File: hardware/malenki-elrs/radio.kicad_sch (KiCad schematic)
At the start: 13 parts, among them U3 SX1280IMLTRT, Y2 CRYSTAL 52MHz 10pF SMD

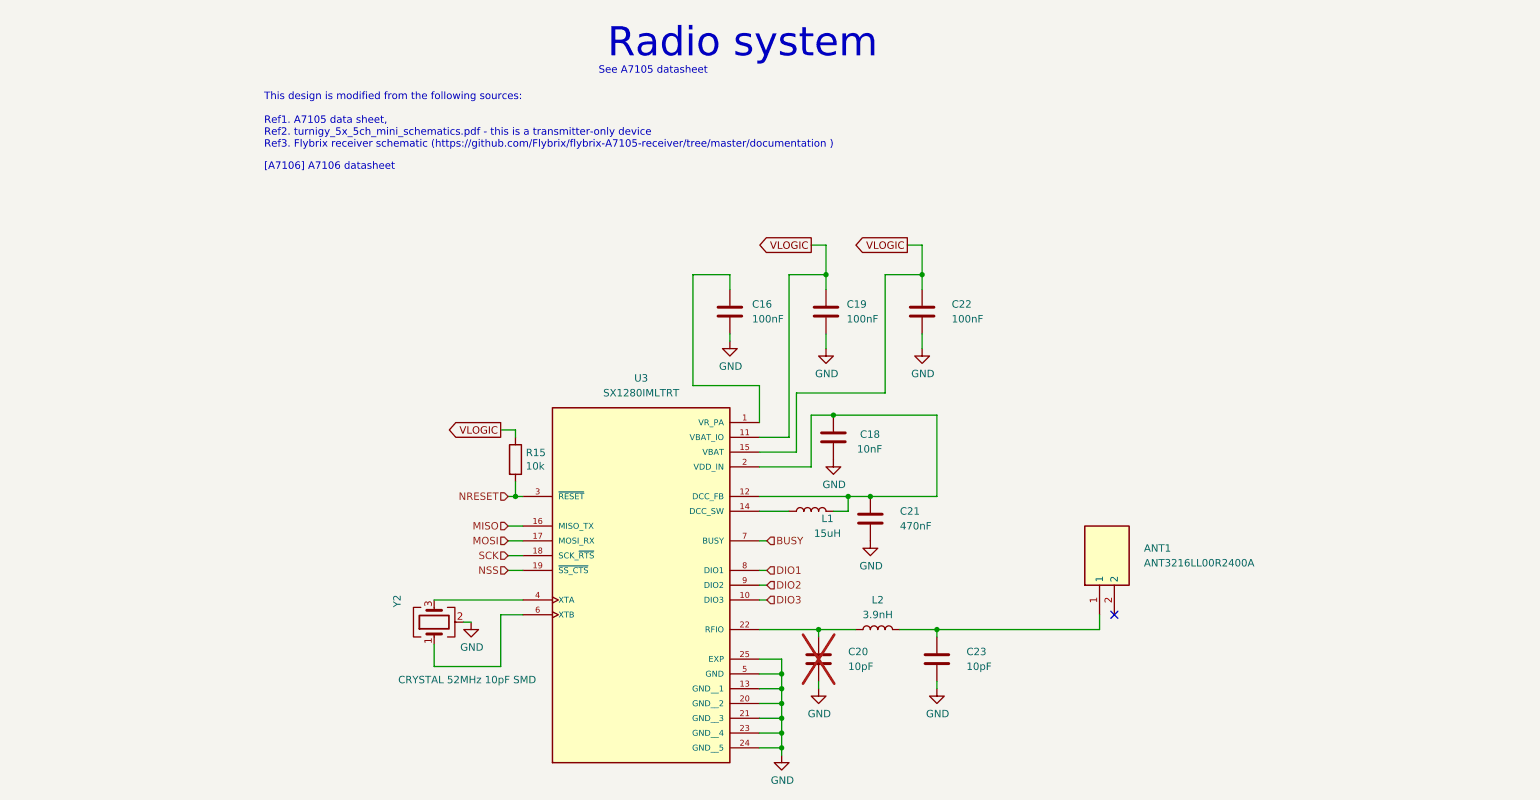
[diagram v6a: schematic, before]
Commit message: Changed microcontroller and completed schematic
Changed micro controller to the esp32-s3FN8, for more available pins.
Complete schematic.
Changed to pcb antenna.
Completed initial placement of all components on PCB.
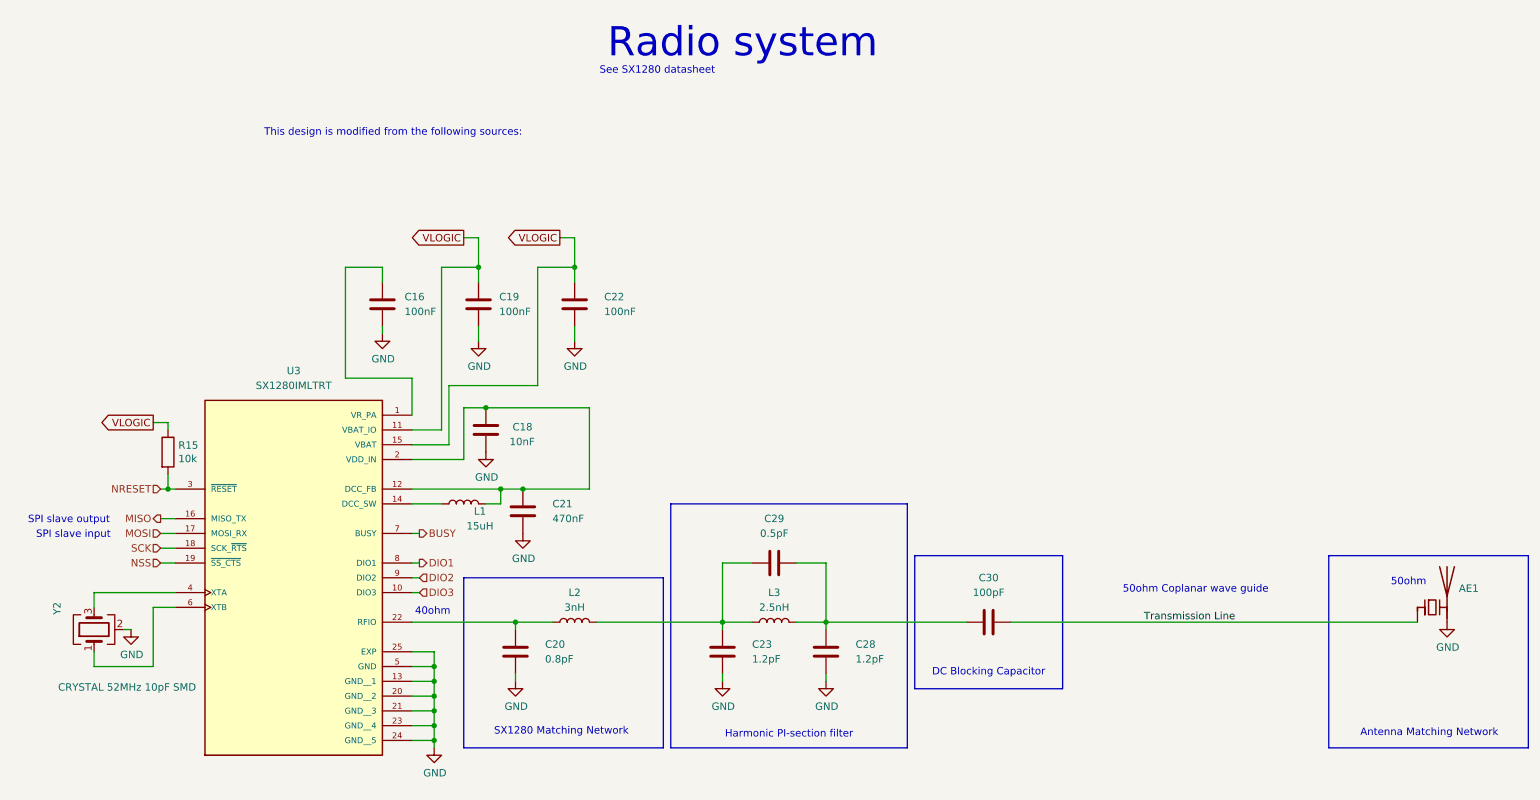
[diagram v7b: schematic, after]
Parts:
- removed ANT1: ANT3216LL00R2400A, malenki-nano:ANT3216LL00R2400A, symbol malenki-elrs:ANT3216LL00R2400A
- added AE1: (no value), malenki-nano:malenki_antenna, symbol Device:Antenna_Chip
- added C28: 1.2pF, Capacitor_SMD:C_0402_1005Metric, symbol Device:C
- added C29: 0.5pF, Capacitor_SMD:C_0402_1005Metric, symbol Device:C
- added C30: 100pF, Capacitor_SMD:C_0402_1005Metric, symbol Device:C
- added L3: 2.5nH, Inductor_SMD:L_0402_1005Metric, symbol Device:L
- C20: value 10pF -> 0.8pF; LCSC C161520 -> C76988; MPN (none) -> GRM1555C1HR80BA01D; now fitted
- C23: value 10pF -> 1.2pF; LCSC C161520 -> (none); MPN (none) -> GRM1555C1H1R2BA01D
- L2: value 3.9nH -> 3nH; LCSC C1330553 -> C2041661; MPN (none) -> LQW15AN3N0B80D
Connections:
- net GND: now also AE1.2 (PCB_Trace), C28.2
- net at C23.1, L2.2: now also C29.1, L3.1
- new net: C28.1, C29.2, C30.1, L3.2
- new net Transmission Line: AE1.1 (FEED), C30.2
- no-connect marks 1 -> 0
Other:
- note added: "40ohm"
- note added: "50ohm"
- note added: "50ohm Coplanar wave guide"
- note added: "Antenna Matching Network"
- note added: "DC Blocking Capacitor"
- note added: "Harmonic PI-section filter"
- note added: "SPI slave input"
- note added: "SPI slave output"
- note added: "SX1280 Matching Network"
- note added: "See SX1280 datasheet"
- note added: "This design is modified from the following sources:"
- note removed: "See A7105 datasheet"
- note removed: "This design is modified from the following sources: Ref1. A7105 data sheet, Ref2. turnigy_5x_5ch_mini_schematics.pdf - this is a transmitter-only device Ref3. Flybrix receiver schematic (https://github.com/Flybrix/flybrix-A7105-receiver/tree/master/documentation )"
- note removed: "[A7106] A7106 datasheet"
- moved on the sheet: C16, C18, C19, C21, C22, C23, L1, L2, R15, U3, Y2

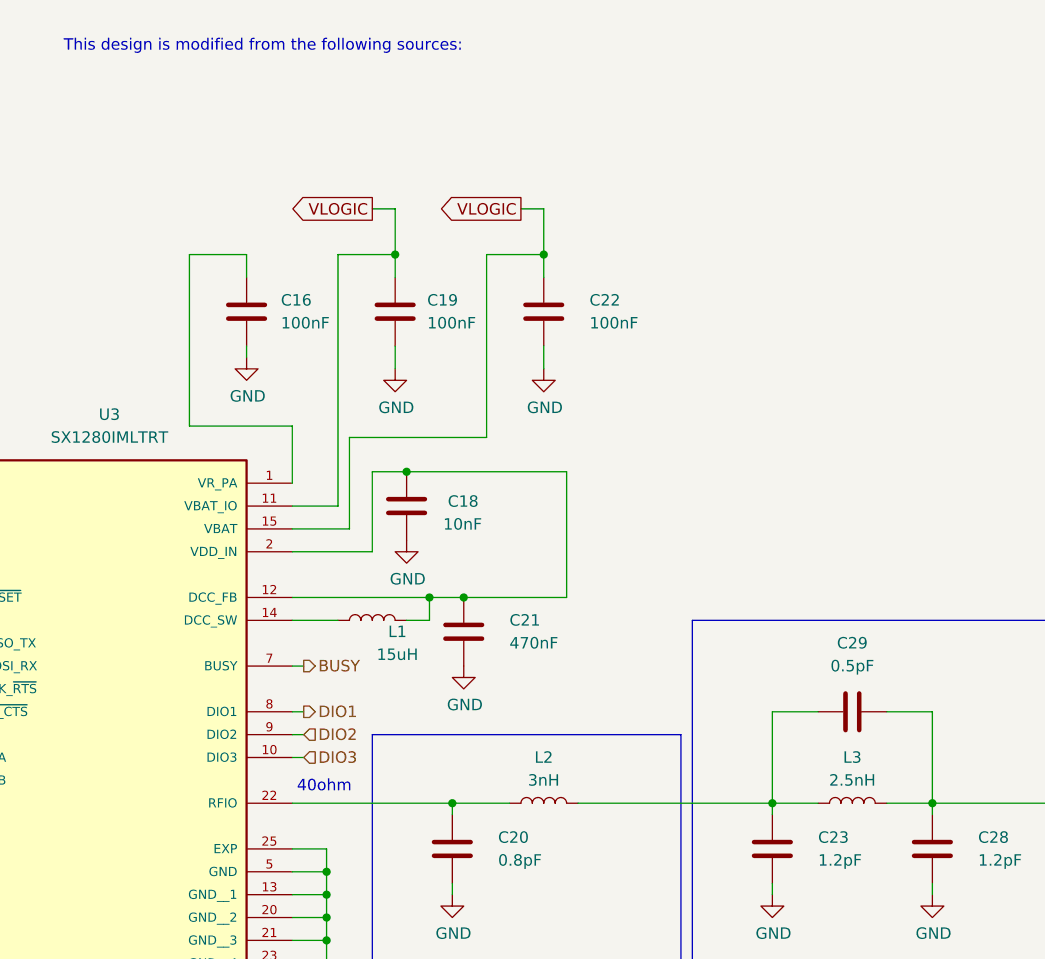
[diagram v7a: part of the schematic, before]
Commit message: Changed component parts to match JLCPCB basic parts
Saving assembly cost by changing all possible components to JLCPCB basic part, and reducing number of separate components where possible. Started trace placement
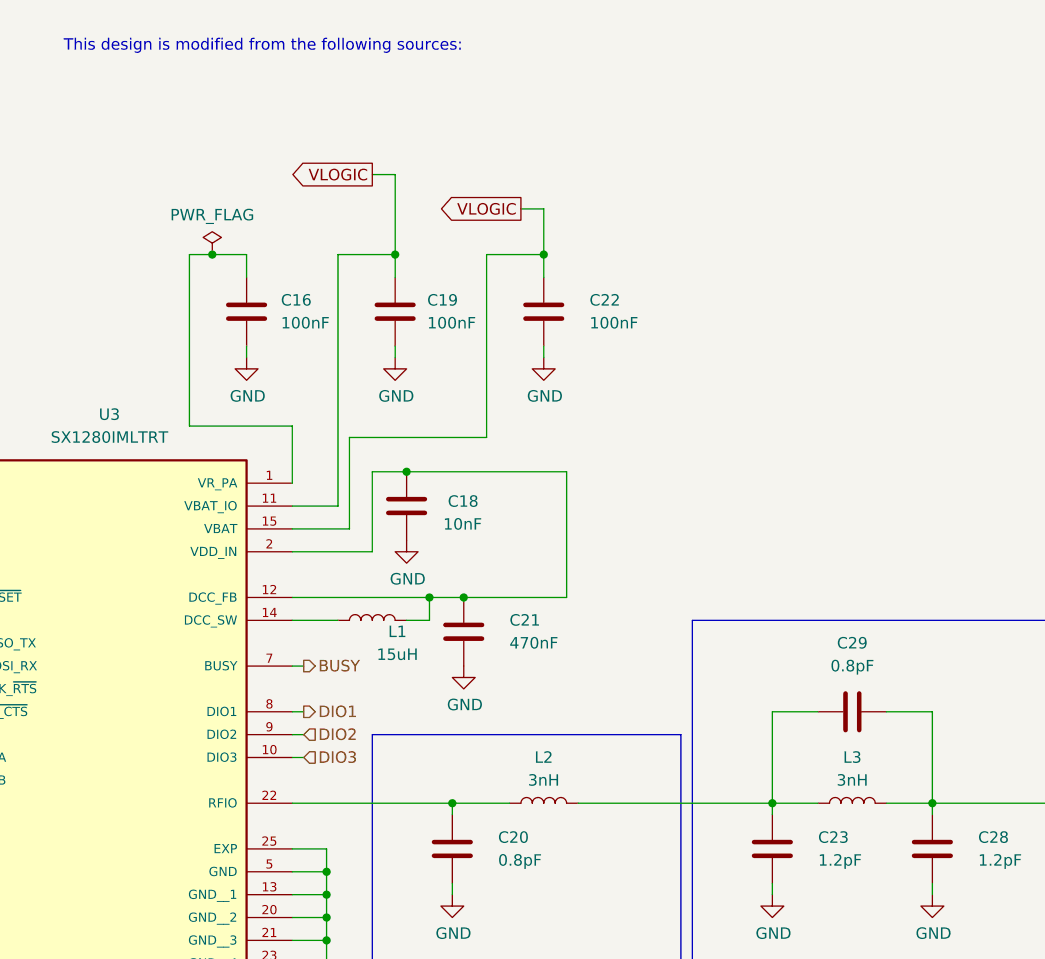
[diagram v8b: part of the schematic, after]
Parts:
- C16, C19, C22: LCSC C100072 -> C1525; MPN (none) -> CL05B104KO5NNNC
- C21: LCSC C92361 -> C47339; MPN (none) -> CL05A474KP5NNNC
- C23, C28: LCSC (none) -> C76899; MPN GRM1555C1H1R2BA01D -> GJM1555C1H1R2WB01D
- C29: value 0.5pF -> 0.8pF; LCSC (none) -> C76988; MPN GRM1555C1HR50WA01D -> GRM1555C1HR80BA01D
- C30: LCSC (none) -> C77177
- L3: value 2.5nH -> 3nH; LCSC (none) -> C2041661; MPN LQW15AN2N5C00D -> LQW15AN3N0B80D
- R15: LCSC C71617 -> C25744; Manufacturer VISHAY -> (none); Partnum CRCW040210K0FKED -> 0402WGF1002TCE
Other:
- note removed: "40ohm"
